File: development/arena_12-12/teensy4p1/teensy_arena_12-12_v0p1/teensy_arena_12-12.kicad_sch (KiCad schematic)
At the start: 0 parts

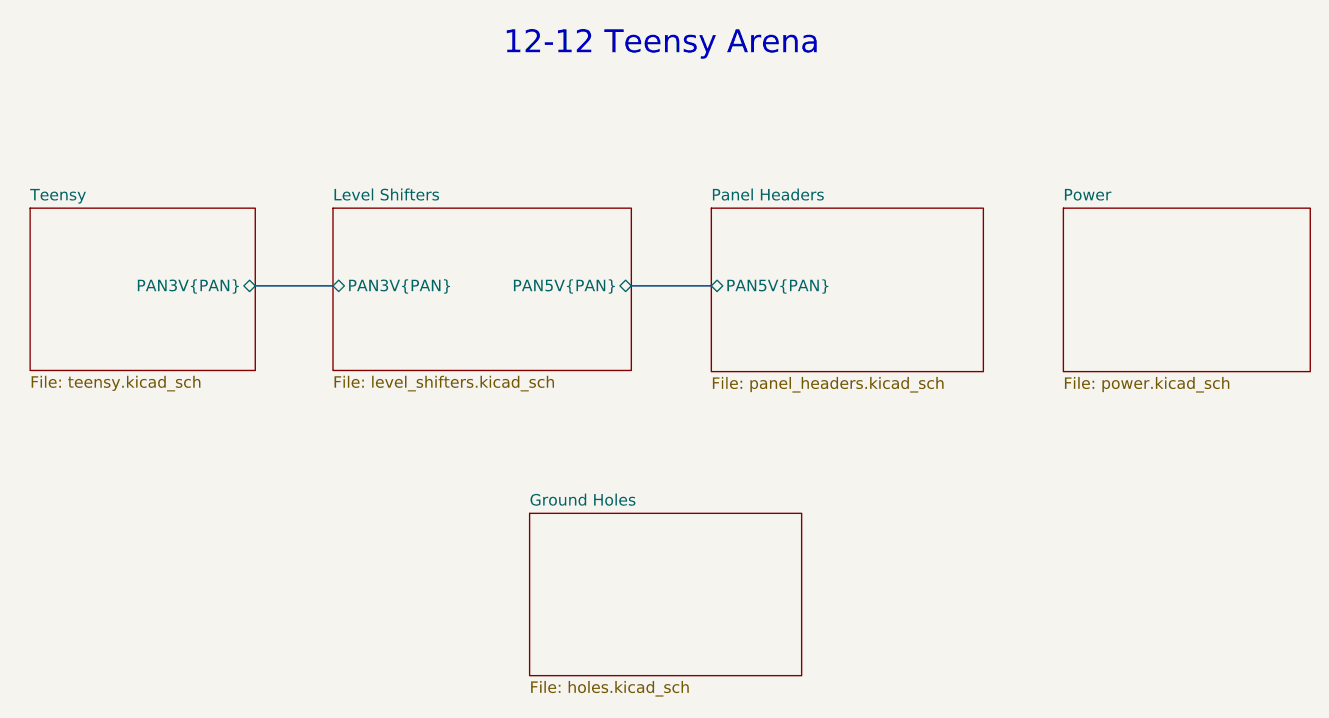
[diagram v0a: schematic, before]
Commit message: Worked on 12-12 teensy4p1 arena without vreg.
Modified SPI connections from teensy to panel columns so that all
signals go from a single source to a single destinatin. Also, added
source termination resistors and schmitt trigger buffers to all SPI
signals.
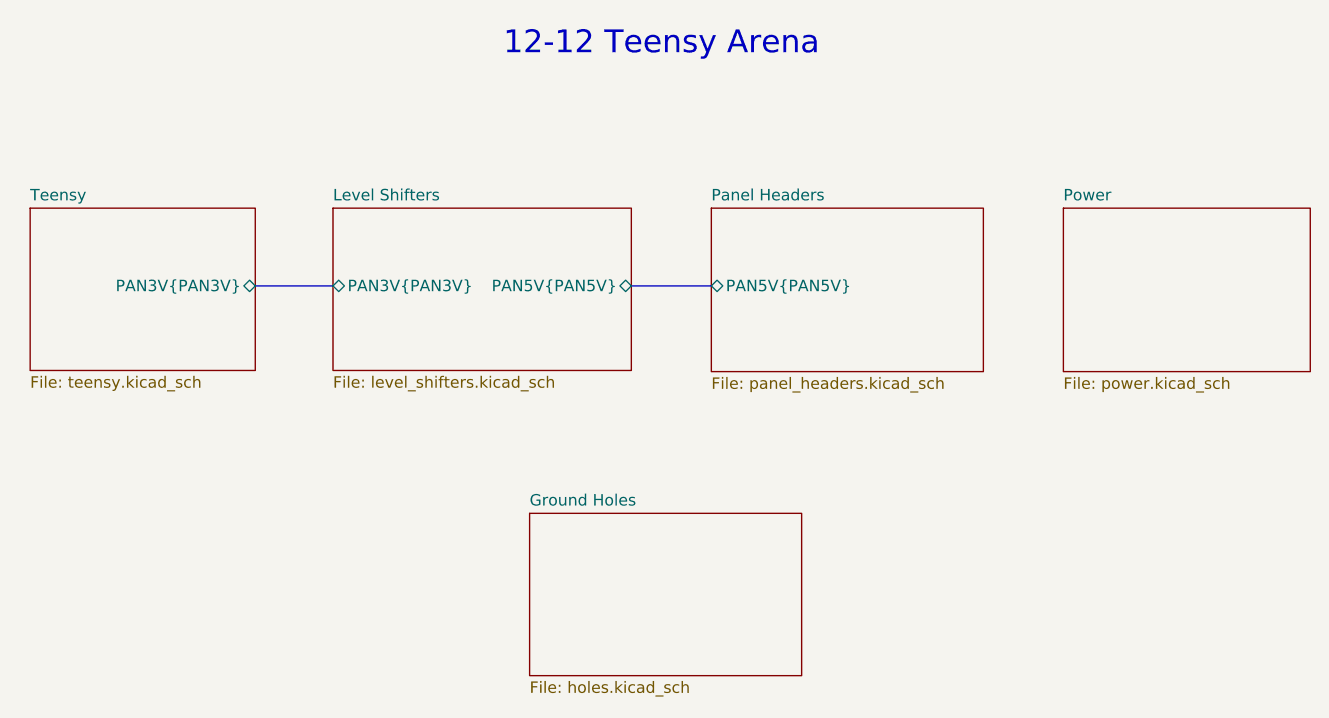
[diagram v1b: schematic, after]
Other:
- sheet Level Shifters ports: added PAN3V{PAN3V}, PAN5V{PAN5V}; removed PAN3V{PAN}, PAN5V{PAN}
- sheet Panel Headers ports: added PAN5V{PAN5V}; removed PAN5V{PAN}
- sheet Teensy ports: added PAN3V{PAN3V}; removed PAN3V{PAN}

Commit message: More work on schematic for 12-12 teensy arena.
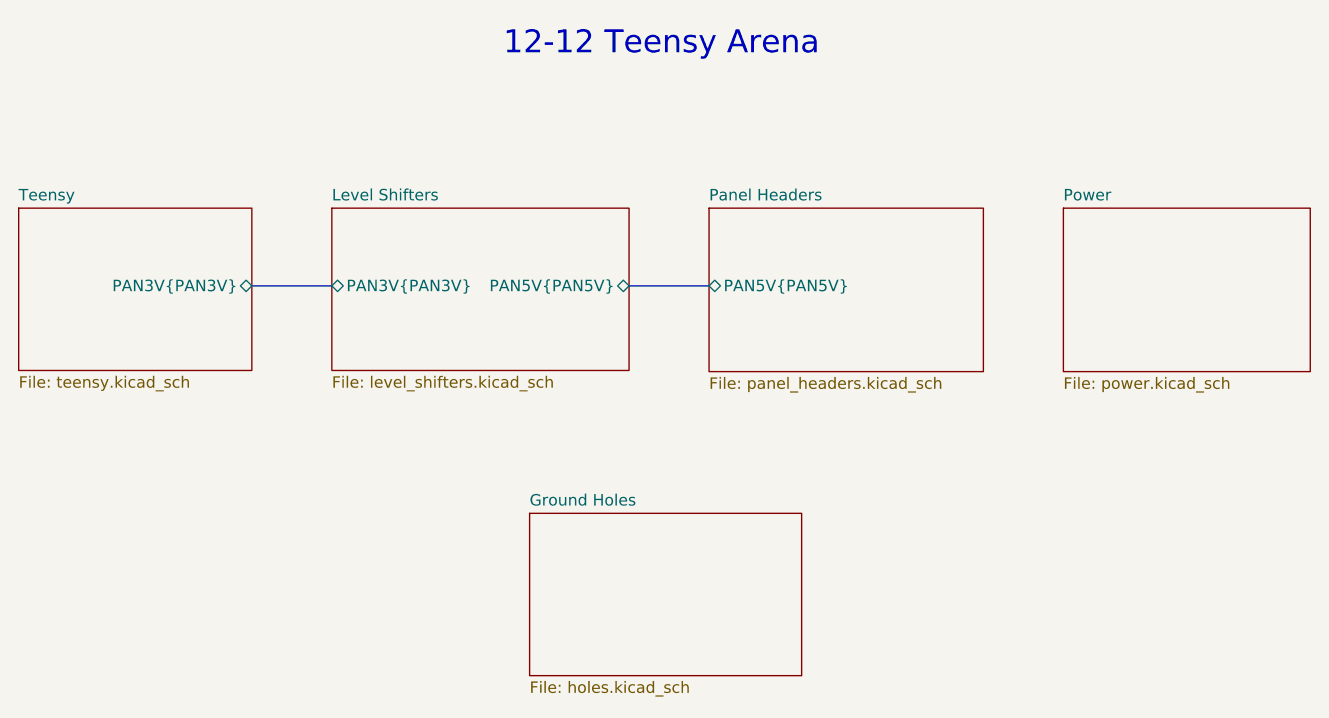
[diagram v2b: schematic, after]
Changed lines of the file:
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@@
 	(bus
 		(pts
-			(xy 127.254 58.42) (xy 136.144 58.42)
+			(xy 85.09 58.42) (xy 93.98 58.42)
 		)
 		(stroke
@@
 	(bus
 		(pts
-			(xy 85.471 58.42) (xy 94.107 58.42)
+			(xy 127 58.42) (xy 135.89 58.42)
 		)
 		(stroke
@@
 	)
 	(sheet
-		(at 94.107 49.784)
-		(size 33.147 18.034)
+		(at 93.98 49.784)
+		(size 33.02 18.034)
 		(fields_autoplaced yes)
 		(stroke
@@
 		)
 		(property "Sheetname" "Level Shifters"
-			(at 94.107 49.0724 0)
+			(at 93.98 49.0724 0)
 			(effects
 				(font
@@
 		)
 		(property "Sheetfile" "level_shifters.kicad_sch"
-			(at 94.107 68.4026 0)
+			(at 93.98 68.4026 0)
 			(effects
 				(font
@@
 		)
 		(pin "PAN5V{PAN5V}" bidirectional
-			(at 127.254 58.42 0)
+			(at 127 58.42 0)
 			(effects
 				(font
@@
 		)
 		(pin "PAN3V{PAN3V}" bidirectional
-			(at 94.107 58.42 180)
+			(at 93.98 58.42 180)
 			(effects
 				(font
@@
 	)
 	(sheet
-		(at 60.452 49.784)
-		(size 25.019 18.034)
+		(at 59.182 49.784)
+		(size 25.908 18.034)
 		(fields_autoplaced yes)
 		(stroke
@@
 		)
 		(property "Sheetname" "Teensy"
-			(at 60.452 49.0724 0)
+			(at 59.182 49.0724 0)
 			(effects
 				(font
@@
 		)
 		(property "Sheetfile" "teensy.kicad_sch"
-			(at 60.452 68.4026 0)
+			(at 59.182 68.4026 0)
 			(effects
 				(font
@@
 		)
 		(pin "PAN3V{PAN3V}" bidirectional
-			(at 85.471 58.42 0)
+			(at 85.09 58.42 0)
 			(effects
 				(font
@@
 	)
 	(sheet
-		(at 136.144 49.784)
-		(size 30.226 18.161)
+		(at 135.89 49.784)
+		(size 30.48 18.161)
 		(fields_autoplaced yes)
 		(stroke
@@
 		)
 		(property "Sheetname" "Panel Headers"
-			(at 136.144 49.0724 0)
+			(at 135.89 49.0724 0)
 			(effects
 				(font
@@
 		)
 		(property "Sheetfile" "panel_headers.kicad_sch"
-			(at 136.144 68.5296 0)
+			(at 135.89 68.5296 0)
 			(effects
 				(font
@@
 		)
 		(pin "PAN5V{PAN5V}" bidirectional
-			(at 136.144 58.42 180)
-			(effects
-				(font
+			(at 135.89 58.42 180)
+			(effects
+				(font
